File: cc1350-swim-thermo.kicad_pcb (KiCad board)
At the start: 2 copper layers, 68.6 x 68.6 mm, 62 parts, among them P1 LMT_70_1, P2 LMT_70_2, P3 SMA FEMALE, P4 USB_OTG, P5 CONN_02X05, Q1 2N7002, SW1 SW_Push, U1 2450BM14G0011T, U2 XMSSJE3G0PA-003, U3 CC1350F128RSM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

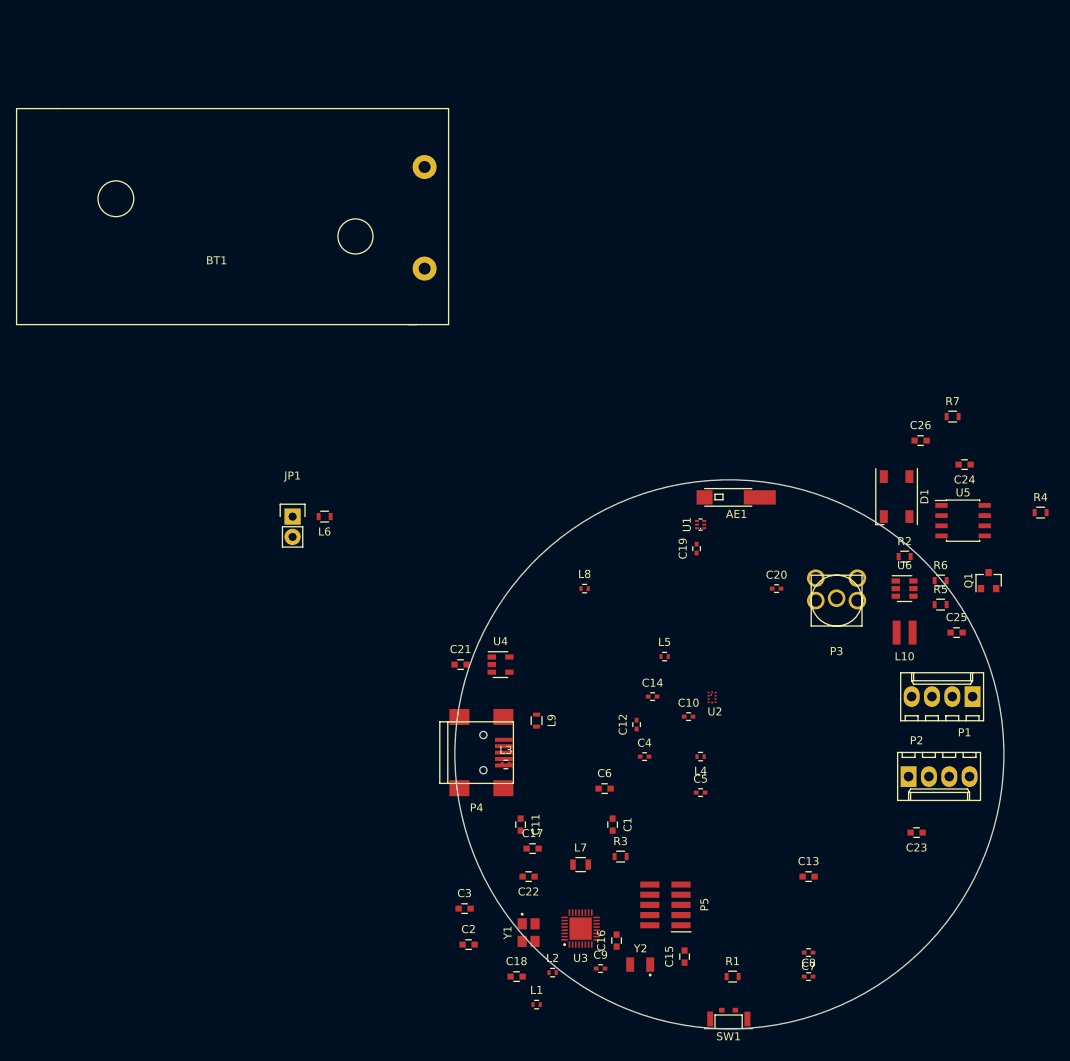
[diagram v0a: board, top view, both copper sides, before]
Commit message: changed balun to LFB18868MBG9E212
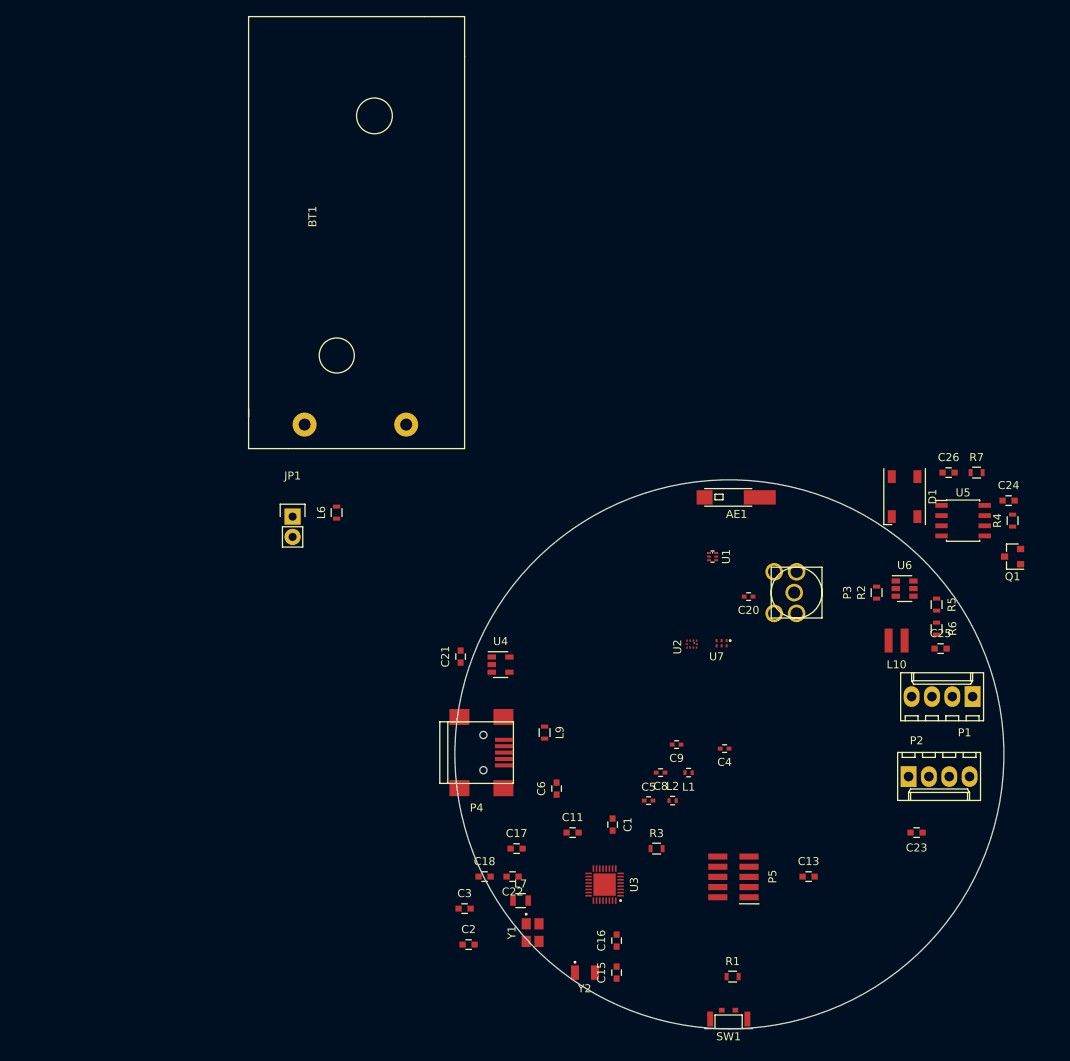
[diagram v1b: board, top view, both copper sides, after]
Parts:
- removed C10, C7: 3.6pF, Capacitors_SMD:C_0402
- removed C12: 3pF, Capacitors_SMD:C_0402
- removed C14: 6.8pF, Capacitors_SMD:C_0402
- removed C19: 3.3pF, Capacitors_SMD:C_0402
- removed L3, L4, L5, L8: 6.8nH, Resistors_SMD:R_0402
- added U7: LFB18868MBG9E212, cc1350:LFB18868MBG9E212, F.Cu at (100.0, 95.0)
- moved L1 34.7 mm to (96.5, 111.5), turned to 180 degrees
- moved C8 31.5 mm to (93.0, 111.5), turned to 180 degrees
- moved C9 29.6 mm to (95.0, 108.0), turned to 180 degrees
- moved L2 26.2 mm to (94.5, 115.0)
- moved BT1 24.6 mm to (48.5, 68.0), turned to 270 degrees
- moved C18 13.1 mm to (71.0, 124.5)
- moved C4 10.0 mm to (101.0, 108.5), turned to 180 degrees
- moved P5 9.19 mm to (102.0, 124.5)
- moved L7 8.75 mm to (75.5, 127.5)
- moved C15 8.73 mm to (87.5, 136.5)
- moved R7 7.62 mm to (132.5, 74.0)
- moved C24 7.11 mm to (136.5, 77.5), turned to 0 degrees
- moved Y2 7.07 mm to (83.5, 136.5), turned to 0 degrees
- moved U2 6.67 mm to (97.5, 95.0), turned to 270 degrees
- moved C11 6.58 mm to (82.0, 119.0), turned to 0 degrees
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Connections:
- P4 pad 2: Net-(P4-Pad2) -> (no net)
- P4 pad 3: Net-(P4-Pad3) -> (no net)
- P4 pad 4: Net-(P4-Pad4) -> (no net)
- P5 pad 7: Net-(P5-Pad7) -> (no net)
- U1 pad 2: Net-(U1-Pad2) -> (no net)
- U4 pad 4: Net-(U4-Pad4) -> (no net)
- U5 pad 5: Net-(U5-Pad5) -> (no net)

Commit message: placed all footprints and new board edge
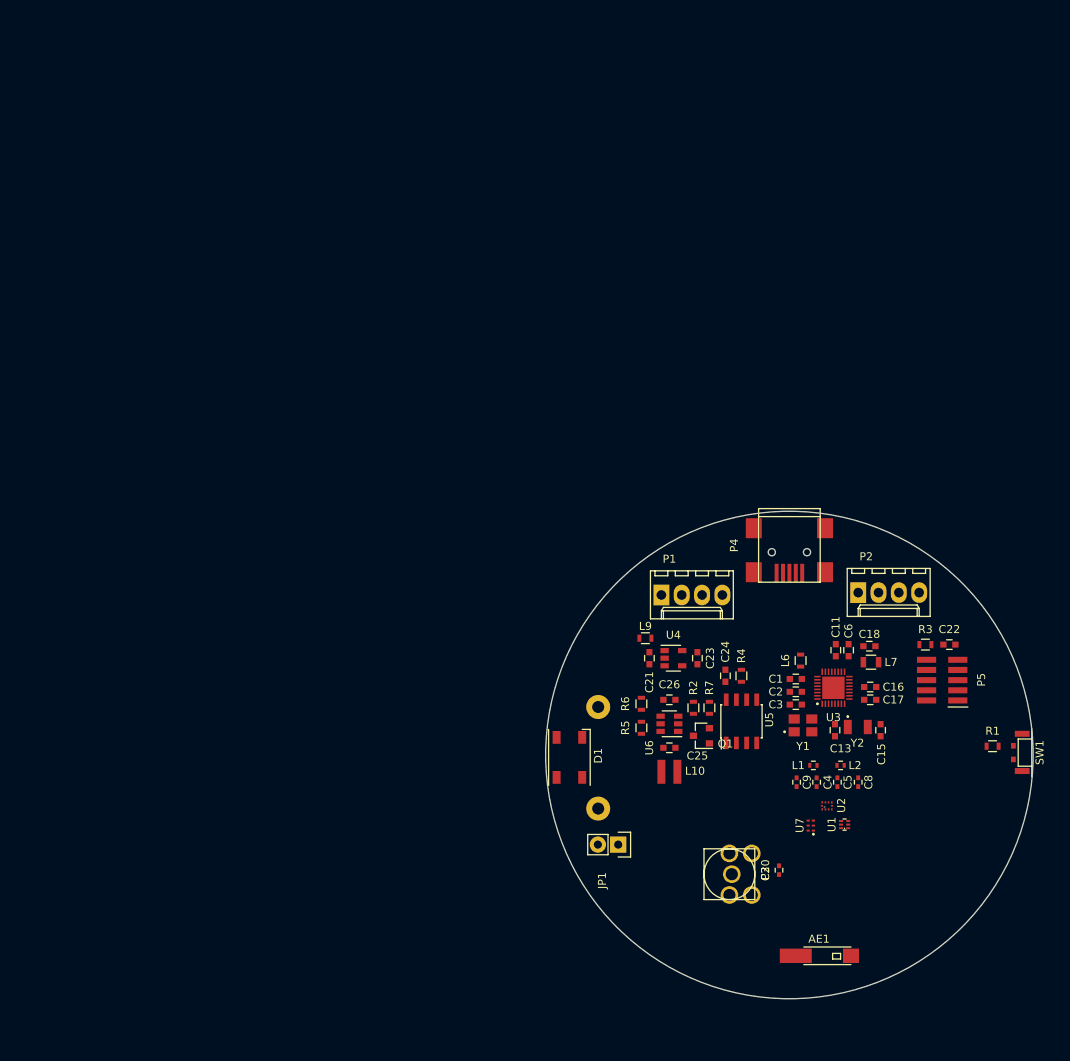
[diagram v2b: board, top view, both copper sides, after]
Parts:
- BT1: moved to B.Cu
- moved C22 61.8 mm to (129.1, 95.5), turned to 0 degrees
- moved L6 60.9 mm to (110.5, 97.5)
- moved BT1 60.4 mm to (85.2, 116.0), turned to 180 degrees
- moved JP1 57.8 mm to (87.7, 120.5), turned to 270 degrees
- moved AE1 56.4 mm to (112.8, 133.5), turned to 180 degrees
- moved C18 56.1 mm to (119.1, 95.7), turned to 180 degrees
- moved D1 53.1 mm to (81.6, 109.6), turned to 90 degrees
- moved L7 53.0 mm to (119.3, 97.7), turned to 180 degrees
- moved C2 51.7 mm to (109.9, 101.4), turned to 180 degrees
- moved SW1 51.3 mm to (139.4, 109.0), turned to 90 degrees
- moved C3 48.6 mm to (109.9, 103.0), turned to 180 degrees
- moved C17 48.0 mm to (119.2, 102.4), turned to 180 degrees
- moved P4 46.9 mm to (109.1, 83.1), turned to 270 degrees
- moved Y2 45.9 mm to (117.6, 105.8)
- moved C26 45.0 mm to (94.1, 102.4)
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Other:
- board size 68.6 x 68.6 mm -> 60.9 x 60.9 mm

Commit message: started wiring
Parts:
- moved L6 29.3 mm to (88.6, 117.0)
- moved C20 5.27 mm to (103.6, 126.9), turned to 0 degrees
- moved P3 4.80 mm to (97.6, 126.9)
- moved C21 4.65 mm to (90.1, 101.6)
- moved C23 4.65 mm to (96.1, 101.6)
- moved C25 4.65 mm to (92.6, 112.8)
- moved C26 4.65 mm to (92.6, 106.8)
- moved L10 4.65 mm to (92.6, 115.8)
- moved L9 4.65 mm to (89.6, 99.1)
- moved Q1 4.65 mm to (96.6, 111.3)
- moved R2 4.65 mm to (95.6, 107.8)
- moved R5 4.65 mm to (89.1, 110.3)
- moved R6 4.65 mm to (89.1, 107.3)
- moved R7 4.65 mm to (97.6, 107.8)
- moved U4 4.65 mm to (93.1, 101.6)
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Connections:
- U1 pad 2: (no net) -> GND
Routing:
- net Net-(C8-Pad1): track 0.00 -> 19.7 mm, vias 0 -> 2
- net Net-(C5-Pad2): track 0.00 -> 9.55 mm
- net Net-(C4-Pad2): track 0.00 -> 9.54 mm
- net Net-(C4-Pad1): track 0.00 -> 2.39 mm
- net Net-(C5-Pad1): track 0.00 -> 2.38 mm
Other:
- copper layers 2 -> 4
- net class Default: clearance 0.2 -> 0.127
- rule trace_clearance: 0.2 -> 0.127

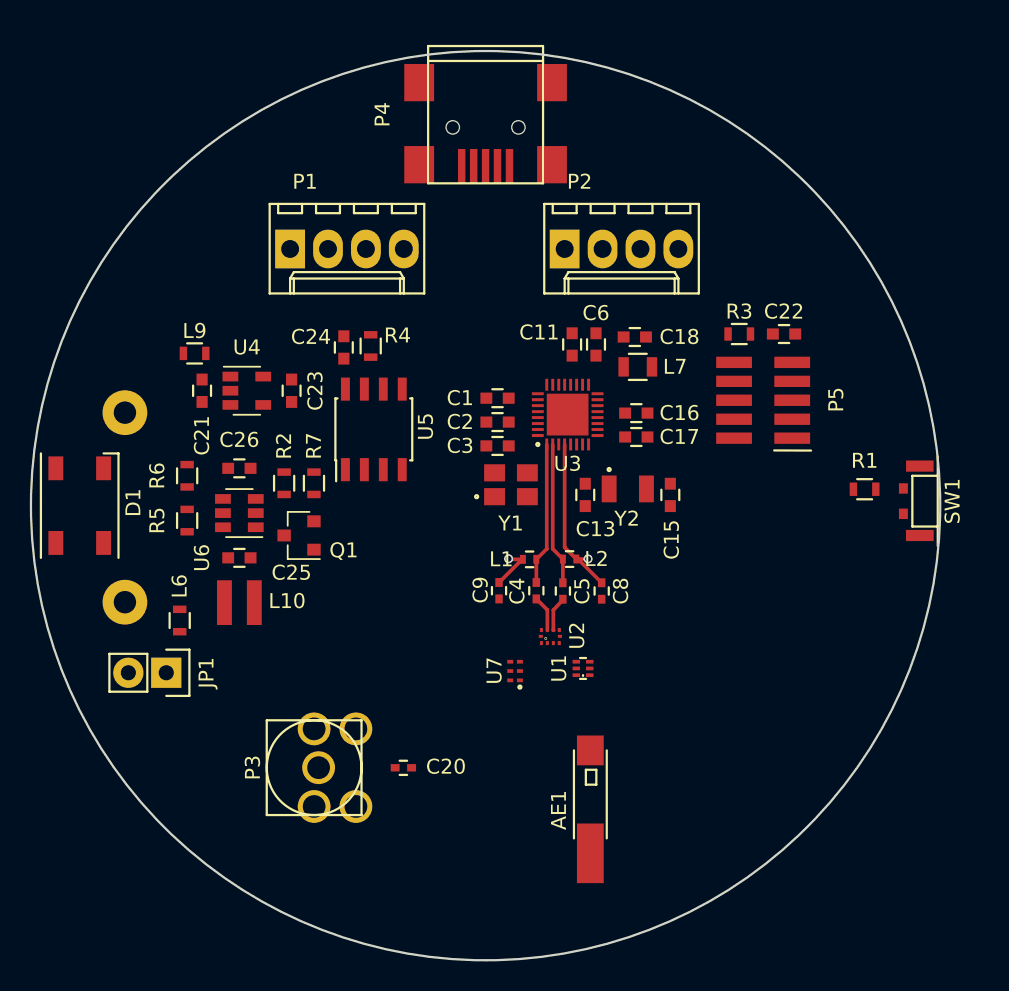
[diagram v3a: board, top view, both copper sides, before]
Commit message: wired all mcu pads
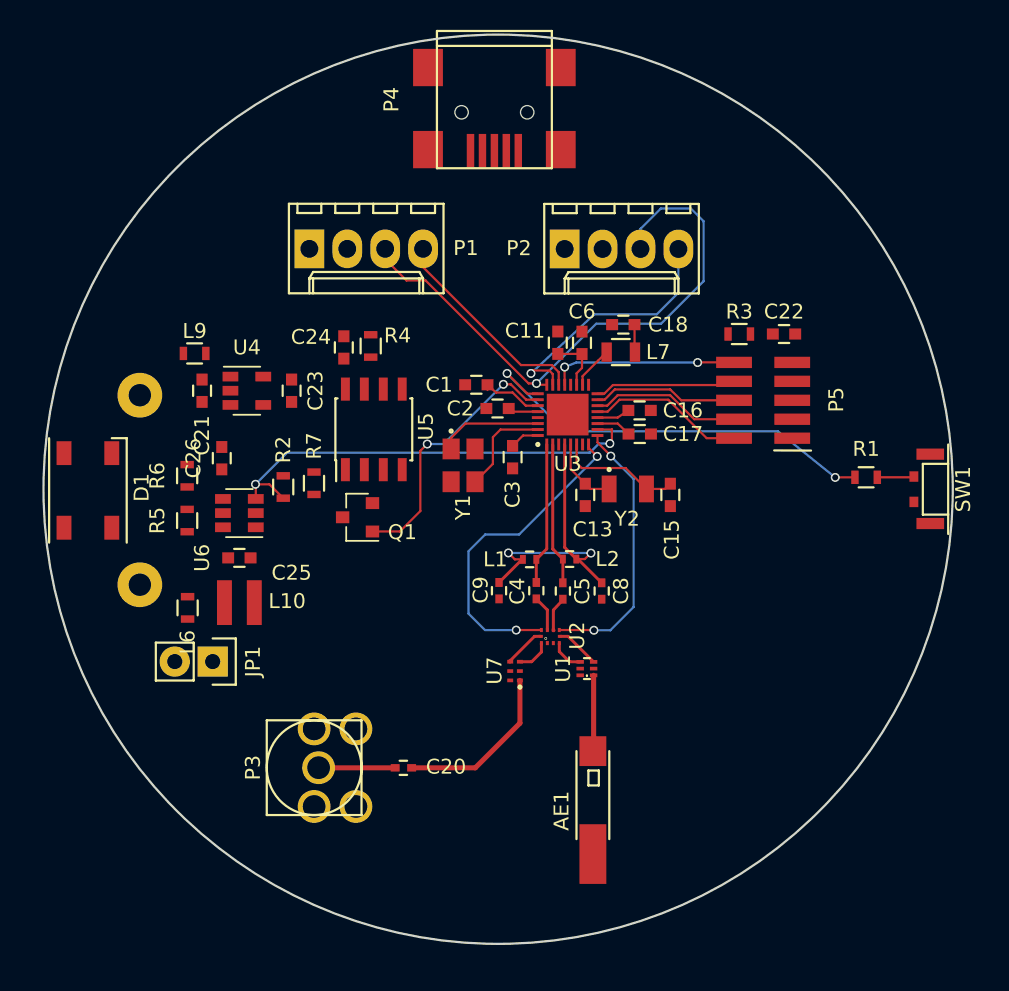
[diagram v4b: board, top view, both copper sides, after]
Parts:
- moved Q1 4.11 mm to (100.5, 110.1)
- moved Y1 3.46 mm to (107.6, 106.6), turned to 270 degrees
- moved JP1 3.20 mm to (90.8, 119.8)
- moved C1 1.68 mm to (108.5, 101.2)
- moved BT1 1.54 mm to (85.9, 114.6)
- moved L7 1.51 mm to (118.2, 99.0)
- moved C26 1.36 mm to (91.4, 106.1), turned to 90 degrees
- moved P1 1.29 mm to (97.3, 92.1)
- moved C3 1.26 mm to (110.9, 106.0), turned to 270 degrees
- moved P4 1.17 mm to (109.7, 82.1)
- moved D1 1.16 mm to (82.5, 108.3)
- moved C18 1.13 mm to (118.3, 97.2)
- moved SW1 1.06 mm to (140.1, 108.2)
- moved L6 1.00 mm to (89.1, 116.2), turned to 270 degrees
- moved C11 0.97 mm to (113.9, 98.4)
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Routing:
- net /TAO: track 0.00 -> 39.6 mm, vias 0 -> 1
- net /PSU_ENABLE: track 0.00 -> 30.1 mm, vias 0 -> 2
- net /SWITCH: track 0.00 -> 28.6 mm, vias 0 -> 2
- net /DIO0_RF_SW_PWR: track 0.00 -> 21.8 mm, vias 0 -> 2
- net /DIO1_RF_SW: track 0.00 -> 18.1 mm, vias 0 -> 2
- net /LED_EASYSET: track 0.00 -> 18.0 mm, vias 0 -> 2
- net /T_ON_2: track 0.00 -> 17.3 mm, vias 0 -> 1
- net /T_ON_1: track 0.00 -> 14.1 mm
- net /RESET_N: track 0.00 -> 12.6 mm, vias 0 -> 2
- net Net-(C20-Pad2): track 0.00 -> 11.4 mm
- net /JTAG_TMSC: track 0.00 -> 10.6 mm
- net /VDDS: track 0.00 -> 10.5 mm
- net /JTAG_TCKC: track 0.00 -> 10.1 mm
- net /JTAG_TDO: track 0.00 -> 9.74 mm
- net /JTAG_TDI: track 0.00 -> 9.49 mm
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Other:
- rule trace_min: 0.2 -> 0.127

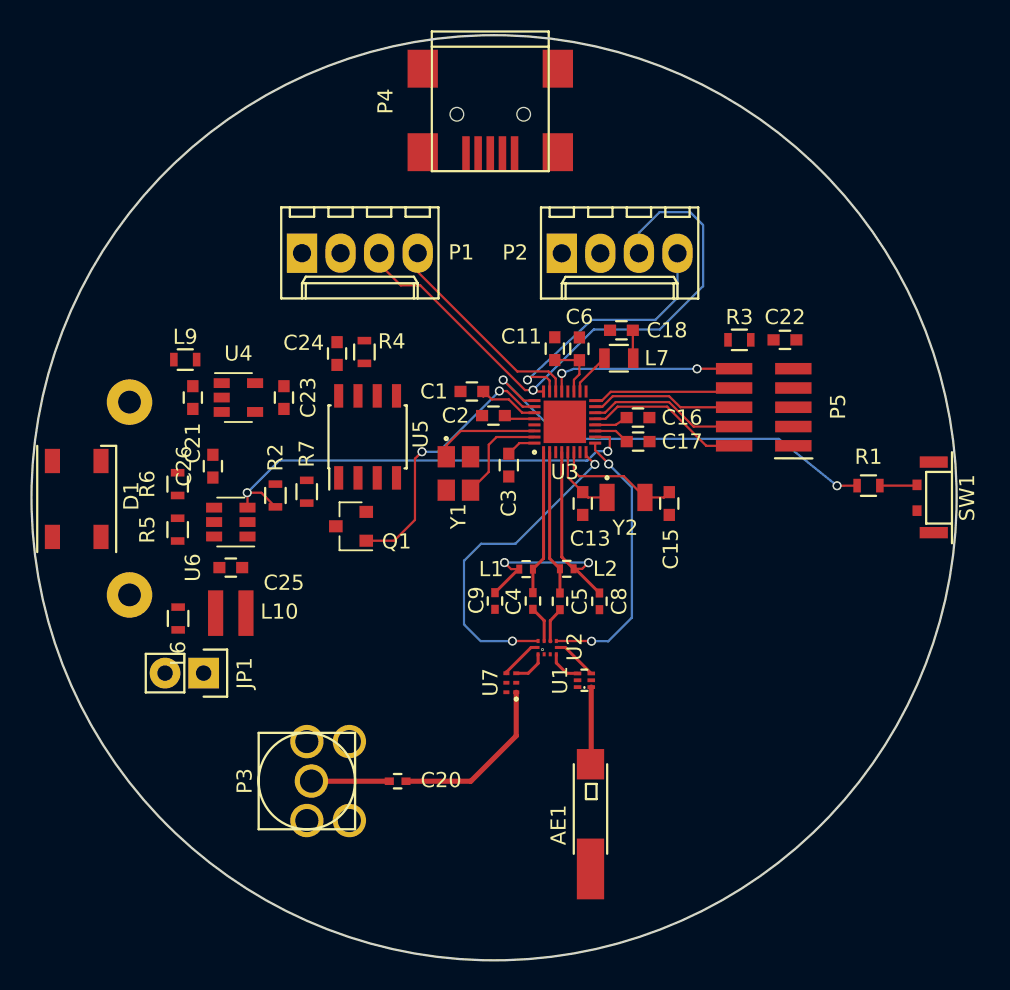
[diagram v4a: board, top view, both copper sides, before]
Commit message: wired all components
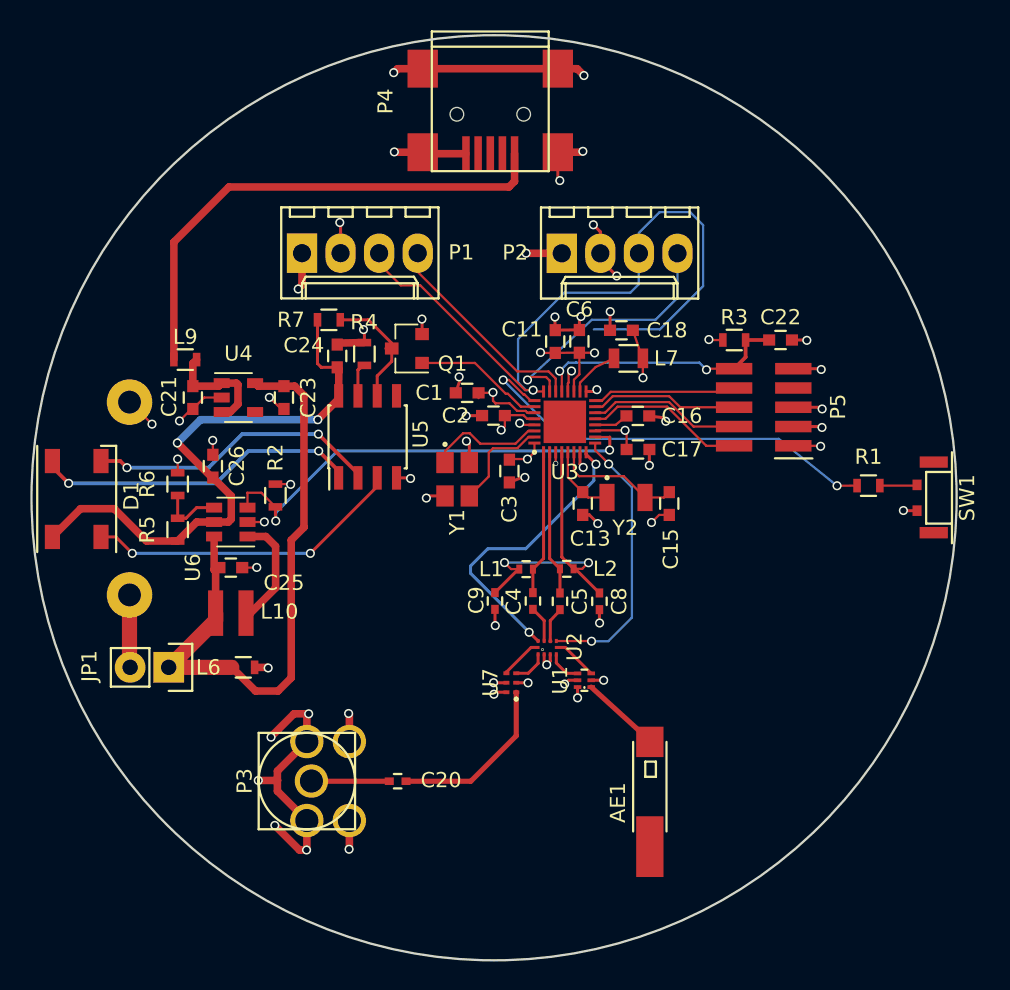
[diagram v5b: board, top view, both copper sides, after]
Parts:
- moved Q1 12.3 mm to (104.2, 98.4)
- moved R7 11.4 mm to (99.1, 96.5), turned to 0 degrees
- moved L6 5.36 mm to (93.4, 119.4), turned to 180 degrees
- moved AE1 4.18 mm to (119.3, 128.3)
- moved JP1 2.33 mm to (88.5, 119.4)
- moved L7 0.63 mm to (118.8, 99.0)
- moved C17 0.52 mm to (119.4, 105.0)
- moved C6 0.49 mm to (115.6, 97.9)
- moved C11 0.47 mm to (114.0, 97.9)
- moved C3 0.39 mm to (111.0, 106.4)
- moved Y1 0.39 mm to (107.5, 107.0)
- moved R3 0.34 mm to (125.8, 97.8)
- moved C1 0.32 mm to (108.2, 101.3)
- moved C22 0.29 mm to (128.8, 97.8)
- moved C24 0.16 mm to (99.6, 98.9)
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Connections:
- P1 pad 1: VCC -> /VDDS
- P2 pad 1: VCC -> /VDDS
- P3 pad 3: (no net) -> GND
- P3 pad 4: (no net) -> GND
- P3 pad 5: (no net) -> GND
- P5 pad 1: VCC -> /VDDS
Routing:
- net GND: track 0.00 -> 312.9 mm, vias 0 -> 57
- net /VDDS: track 10.5 -> 110.5 mm, vias 0 -> 9
- net VCC: track 0.00 -> 41.5 mm
- net +5V: track 0.00 -> 38.8 mm, vias 0 -> 2
- net Net-(L9-Pad2): track 0.00 -> 33.7 mm
- net Net-(D1-Pad4): track 0.00 -> 21.6 mm, vias 0 -> 2
- net Net-(D1-Pad2): track 0.00 -> 21.0 mm, vias 0 -> 2
- net Net-(D1-Pad3): track 0.00 -> 19.4 mm, vias 0 -> 2
- net /VDDR: track 5.87 -> 22.5 mm, vias 0 -> 3
- net /TAO: track 39.6 -> 49.4 mm
- net /LED_EASYSET: track 18.0 -> 8.59 mm, vias 2 -> 0
- net Net-(Q1-Pad3): track 0.00 -> 8.28 mm
- net Net-(C21-Pad2): track 0.00 -> 7.52 mm
- net Net-(L10-Pad1): track 0.00 -> 7.50 mm
- net Net-(BT1-Pad1): track 0.00 -> 4.79 mm
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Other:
- rule via_min_drill: 0.3 -> 0.254
- rule via_min_size: 0.4 -> 0.3
